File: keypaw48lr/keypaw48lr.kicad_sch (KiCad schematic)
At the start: 103 parts, among them J1 Conn_01x02, J2 Conn_01x02, J3 Conn_01x02, J4 Conn_01x02, J5 Conn_01x02, J6 JD9613_OLED_FPC_Conn_01x10, J7 JD9613_OLED_FPC_Conn_01x10, SW1 SW_SPDT, SW2 RotaryEncoder, U1 nice_nano, U2 PAW3395, U3 TLV70019_SOT23-5, U4 TPS22917DBV

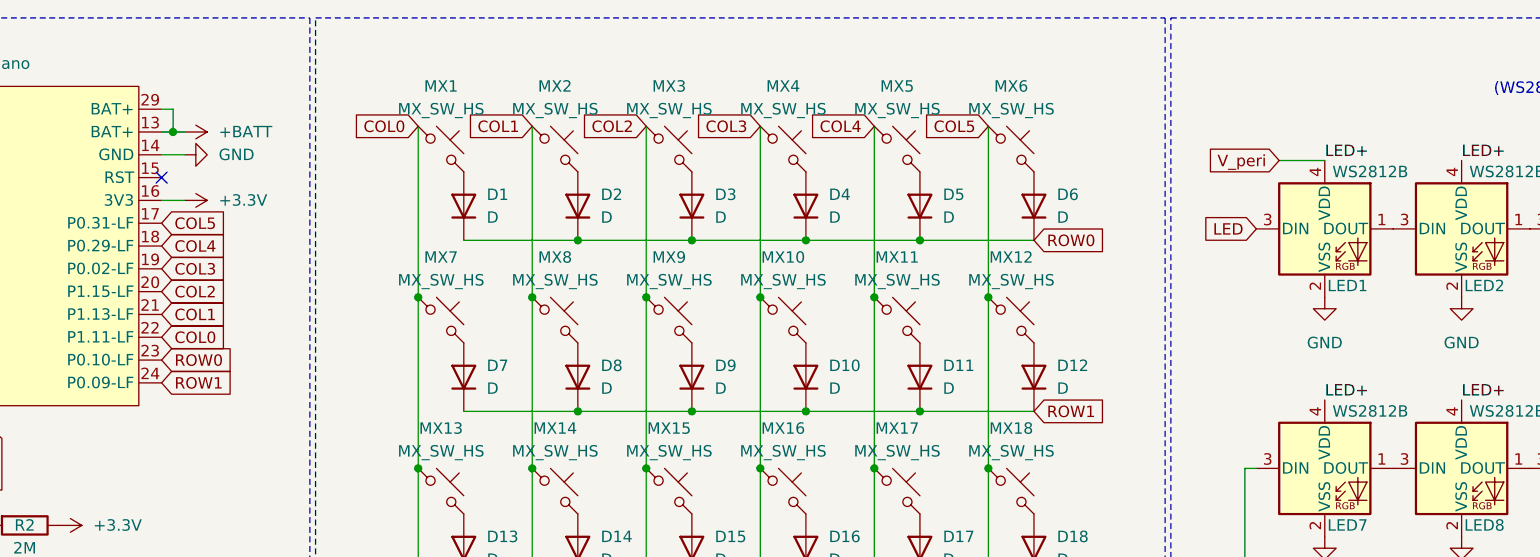
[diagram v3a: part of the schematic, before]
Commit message: feat: group leds with rule areas for multichannel wiring
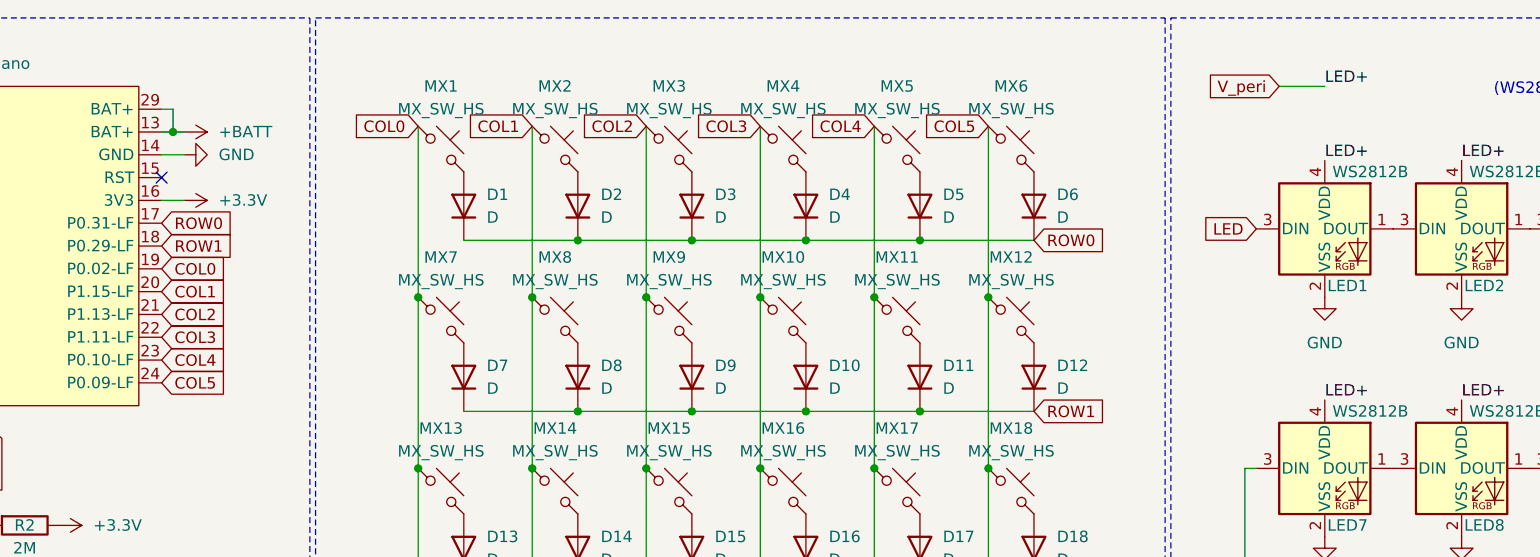
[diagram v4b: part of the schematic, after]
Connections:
- net COL0: now also U1.19 (P0.02-LF); no longer U1.22 (P1.11-LF)
- net COL1: now also U1.20 (P1.15-LF); no longer U1.21 (P1.13-LF)
- net COL2: now also U1.21 (P1.13-LF); no longer U1.20 (P1.15-LF)
- net COL3: now also U1.22 (P1.11-LF); no longer U1.19 (P0.02-LF)
- net COL4: now also U1.23 (P0.10-LF); no longer U1.18 (P0.29-LF)
- net COL5: now also U1.24 (P0.09-LF); no longer U1.17 (P0.31-LF)
- net ROW0: now also U1.17 (P0.31-LF); no longer U1.23 (P0.10-LF)
- net ROW1: now also U1.18 (P0.29-LF); no longer U1.24 (P0.09-LF)

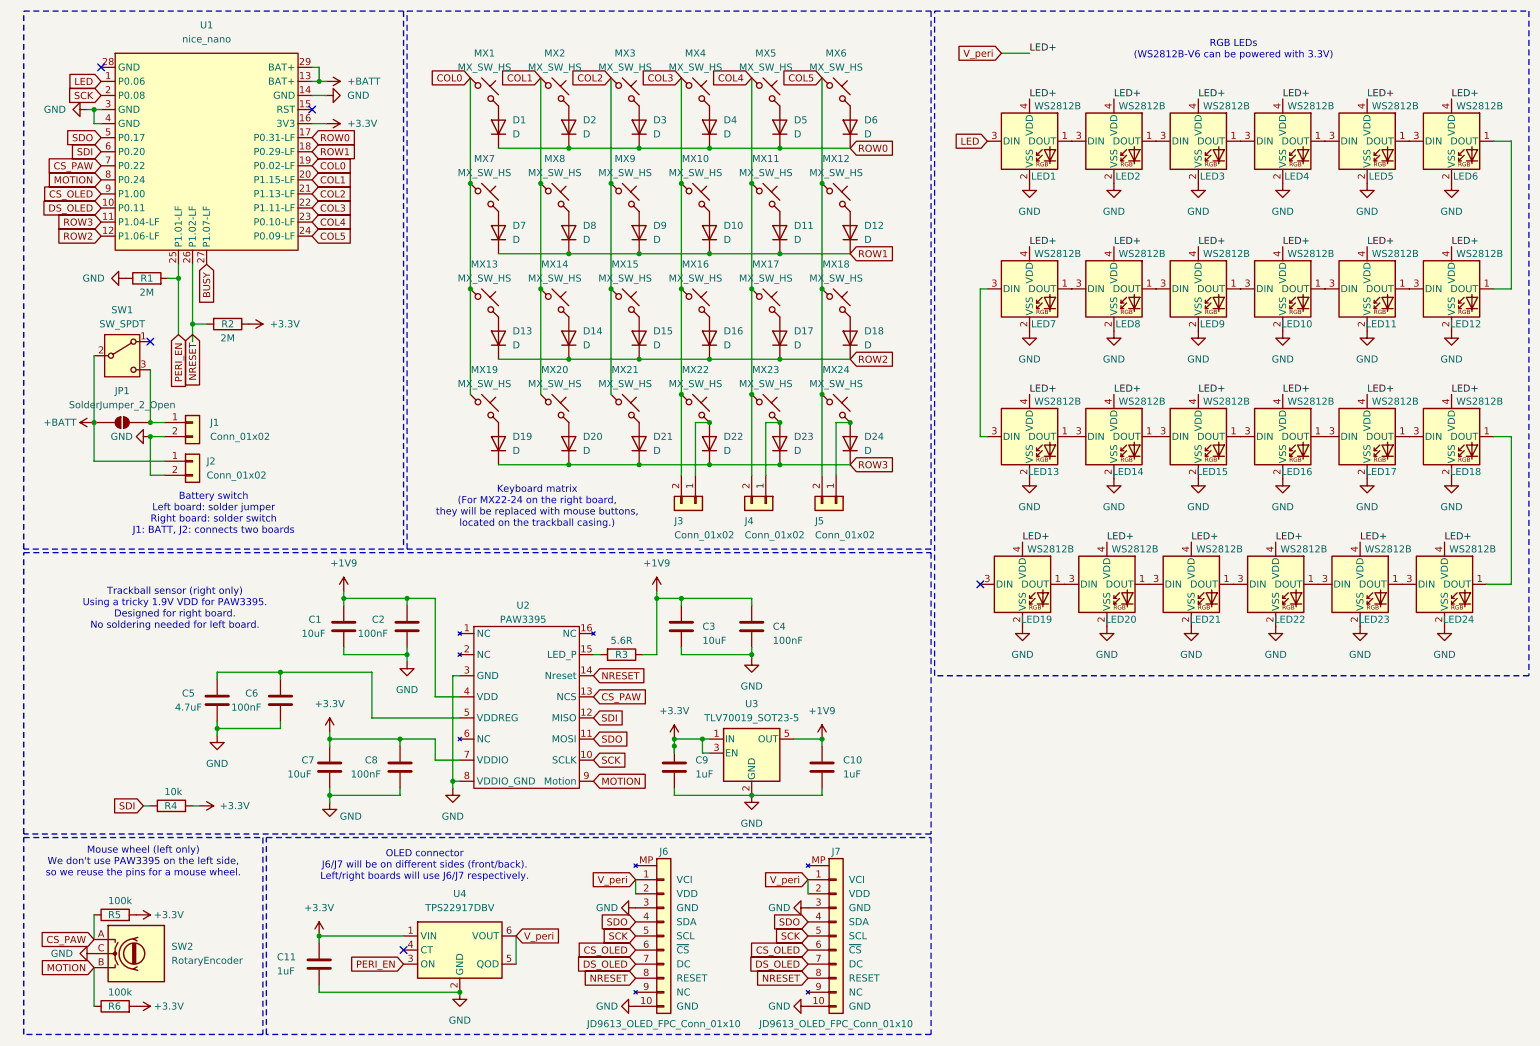
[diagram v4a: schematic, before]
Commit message: feat: basic key matrix wiring
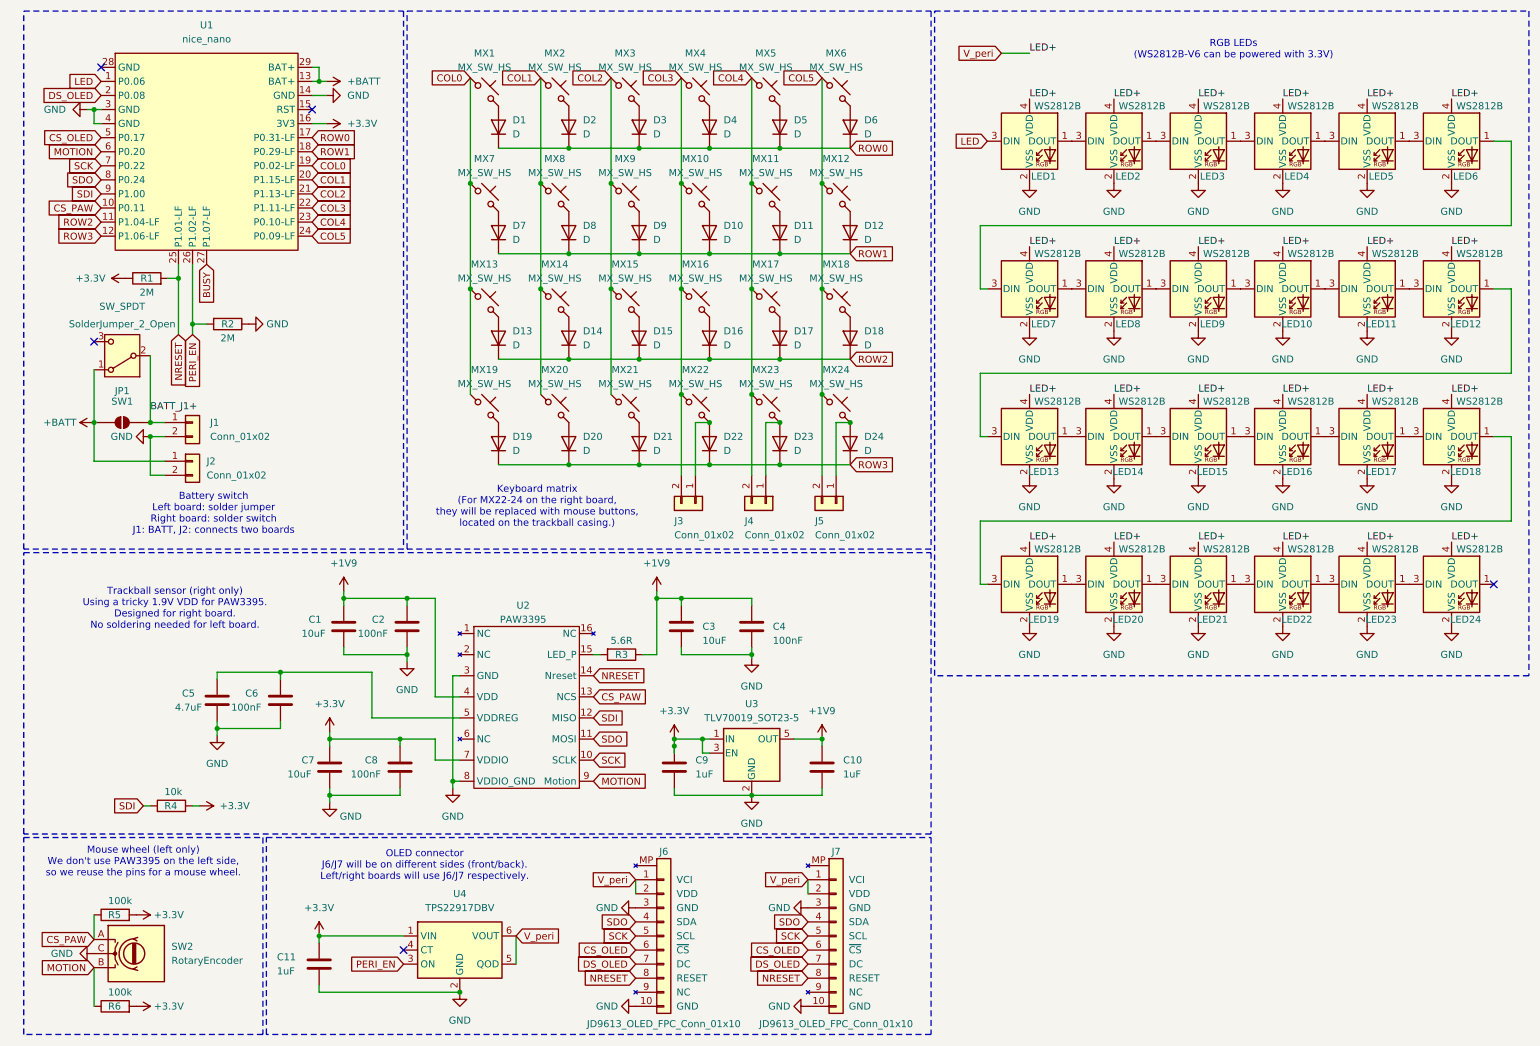
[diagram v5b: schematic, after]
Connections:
- net +3.3V: now also R1.1; no longer R2.1
- net +BATT: now also SW1.1 (A); no longer SW1.2 (B)
- net CS_OLED: now also U1.5 (P0.17); no longer U1.9 (P1.00)
- net CS_PAW: now also U1.10 (P0.11); no longer U1.7 (P0.22)
- net DS_OLED: now also U1.2 (P0.08); no longer U1.10 (P0.11)
- net GND: now also R2.1; no longer R1.1
- net MOTION: now also U1.6 (P0.20); no longer U1.8 (P0.24)
- net NRESET: now also R1.2, U1.25 (P1.01-LF); no longer R2.2, U1.26 (P1.02-LF)
- net PERI_EN: now also R2.2, U1.26 (P1.02-LF); no longer R1.2, U1.25 (P1.01-LF)
- net ROW2: now also U1.11 (P1.04-LF); no longer U1.12 (P1.06-LF)
- net ROW3: now also U1.12 (P1.06-LF); no longer U1.11 (P1.04-LF)
- net SCK: now also U1.7 (P0.22); no longer U1.2 (P0.08)
- net SDI: now also U1.9 (P1.00); no longer U1.6 (P0.20)
- net SDO: now also U1.8 (P0.24); no longer U1.5 (P0.17)
- net at LED18.1 (DOUT): now also LED19.3 (DIN); no longer LED24.1 (DOUT)
- net at LED6.1 (DOUT): now also LED7.3 (DIN); no longer LED12.1 (DOUT)
- net at LED13.3 (DIN): now also LED12.1 (DOUT); no longer LED7.3 (DIN)
- net BATT_J1+: now reaches J1.1 (Pin_1), JP1.2 (B)
- net BATT_J1+: now also SW1.2 (B); no longer SW1.3 (C)
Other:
- moved on the sheet: LED19, LED20, LED21, LED22, LED23, LED24, SW1

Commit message: feat: finish pcb wiring draft
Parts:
- U4: footprint Package_TO_SOT_SMD:SOT-23-6_Handsoldering -> MX_SW_HS_REV:SOT-23-6_Handsoldering_REV
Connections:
- net COL3: now also J3.1 (Pin_1); no longer J3.2 (Pin_2)
- net COL4: now also J4.1 (Pin_1); no longer J4.2 (Pin_2)
- net COL5: now also J5.1 (Pin_1); no longer J5.2 (Pin_2)
- net at D24.2 (A), MX24.2: now also J5.2 (Pin_2); no longer J5.1 (Pin_1)
- net at D22.2 (A), MX22.2: now also J3.2 (Pin_2); no longer J3.1 (Pin_1)
- net at D23.2 (A), MX23.2: now also J4.2 (Pin_2); no longer J4.1 (Pin_1)
- net PAW_VDD: now reaches C5.1, C6.1, U2.5 (VDDREG)
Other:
- moved on the sheet: J3, J4, J5
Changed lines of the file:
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@@
 		)
 	)
+	(label "PAW_VDD"
+		(at 47.625 132.08 0)
+		(effects
+			(font
+				(size 1.27 1.27)
+			)
+			(justify left bottom)
+		)
+	)
 	(label "LED+"
 		(at 270.51 55.245 0)
@@
 	(symbol
 		(lib_id "Connector_Generic:Conn_01x02")
-		(at 159.385 101.6 270)
+		(at 156.845 101.6 90)
+		(mirror x)
 		(unit 1)
 		(body_style 1)
@@
 		(dnp no)
 		(property "Reference" "J5"
-			(at 155.575 104.775 90)
+			(at 160.655 104.775 90)
 			(show_name no)
 			(do_not_autoplace no)
@@
 		)
 		(property "Value" "Conn_01x02"
-			(at 155.575 107.315 90)
+			(at 160.655 107.315 90)
 			(show_name no)
 			(do_not_autoplace no)
@@
 		)
 		(property "Footprint" "Connector_Molex:Molex_PicoBlade_53048-0210_1x02_P1.25mm_Horizontal"
-			(at 159.385 101.6 0)
+			(at 156.845 101.6 0)
 			(hide yes)
 			(show_name no)
@@
 		)
 		(property "Datasheet" ""
-			(at 159.385 101.6 0)
+			(at 156.845 101.6 0)
 			(hide yes)
 			(show_name no)
@@
 		)
 		(property "Description" "Generic connector, single row, 01x02, script generated (kicad-library-utils/schlib/autogen/connector/)"
-			(at 159.385 101.6 0)
+			(at 156.845 101.6 0)
 			(hide yes)
 			(show_name no)
@@
 			)
 		)
-		(property "Footprint" "Package_TO_SOT_SMD:SOT-23-6_Handsoldering"
+		(property "Footprint" "MX_SW_HS_REV:SOT-23-6_Handsoldering_REV"
 			(at 91.44 169.545 0)
 			(hide yes)
@@
 	(symbol
 		(lib_id "Connector_Generic:Conn_01x02")
-		(at 146.685 101.6 270)
+		(at 144.145 101.6 90)
+		(mirror x)
 		(unit 1)
 		(body_style 1)
@@
 		(dnp no)
 		(property "Reference" "J4"
-			(at 142.875 104.775 90)
+			(at 147.955 104.775 90)
 			(show_name no)
 			(do_not_autoplace no)
@@
 		)
 		(property "Value" "Conn_01x02"
-			(at 142.875 107.315 90)
+			(at 147.955 107.315 90)
 			(show_name no)
 			(do_not_autoplace no)
@@
 		)
 		(property "Footprint" "Connector_Molex:Molex_PicoBlade_53048-0210_1x02_P1.25mm_Horizontal"
-			(at 146.685 101.6 0)
+			(at 144.145 101.6 0)
 			(hide yes)
 			(show_name no)
@@
 		)
 		(property "Datasheet" ""
-			(at 146.685 101.6 0)
+			(at 144.145 101.6 0)
 			(hide yes)
 			(show_name no)
@@
 		)
 		(property "Description" "Generic connector, single row, 01x02, script generated (kicad-library-utils/schlib/autogen/connector/)"
-			(at 146.685 101.6 0)
+			(at 144.145 101.6 0)
 			(hide yes)
 			(show_name no)
@@
 	(symbol
 		(lib_id "Connector_Generic:Conn_01x02")
-		(at 133.985 101.6 270)
+		(at 131.445 101.6 90)
+		(mirror x)
 		(unit 1)
 		(body_style 1)
@@
 		(dnp no)
 		(property "Reference" "J3"
-			(at 130.175 104.775 90)
+			(at 135.255 104.775 90)
 			(show_name no)
 			(do_not_autoplace no)
@@
 		)
 		(property "Value" "Conn_01x02"
-			(at 130.175 107.315 90)
+			(at 135.255 107.315 90)
 			(show_name no)
 			(do_not_autoplace no)
@@
 		)
 		(property "Footprint" "Connector_Molex:Molex_PicoBlade_53048-0210_1x02_P1.25mm_Horizontal"
-			(at 133.985 101.6 0)
+			(at 131.445 101.6 0)
 			(hide yes)
 			(show_name no)
@@
 		)
 		(property "Datasheet" ""
-			(at 133.985 101.6 0)
+			(at 131.445 101.6 0)
 			(hide yes)
 			(show_name no)
@@
 		)
 		(property "Description" "Generic connector, single row, 01x02, script generated (kicad-library-utils/schlib/autogen/connector/)"
-			(at 133.985 101.6 0)
+			(at 131.445 101.6 0)
 			(hide yes)
 			(show_name no)

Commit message: fix: should be able to solder nice!nano on both sides
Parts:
- U1: footprint PCM_marbastlib-xp-promicroish:nice_nano_AH_USBup -> MX_SW_HS_REV:nice_nano_AH_USBup_REV
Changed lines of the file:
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@@
 			)
 		)
-		(property "Footprint" "PCM_marbastlib-xp-promicroish:nice_nano_AH_USBup"
+		(property "Footprint" "MX_SW_HS_REV:nice_nano_AH_USBup_REV"
 			(at 45.72 69.85 0)
 			(hide yes)
